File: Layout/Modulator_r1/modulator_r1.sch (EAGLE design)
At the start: 86 parts, among them Q1 FA-20H, U1 ATMEGA328P-AU, U2 TPS79933QDDCRQ1, U3 CC1125RHBT, U4 MCP1700T-3302E/TT, U5 FT232RL, U6 SIP32509DT-T1-GE3

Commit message: Add DTR coupling to reset. Closes #9.
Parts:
- added C34: 100nF, resistor:C-EUC0603
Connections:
- new net N$20: C34.2, U5.!DTR
- net AVR_NRESET: now also C34.1
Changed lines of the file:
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@@
 <grid distance="0.1" unitdist="inch" unit="inch" style="lines" multiple="1" display="no" altdistance="0.01" altunitdist="inch" altunit="inch"/>
 <layers>
-<layer number="1" name="Top" color="4" fill="1" visible="yes" active="no"/>
-<layer number="16" name="Bottom" color="1" fill="1" visible="yes" active="no"/>
-<layer number="17" name="Pads" color="2" fill="1" visible="yes" active="no"/>
-<layer number="18" name="Vias" color="2" fill="1" visible="yes" active="no"/>
-<layer number="19" name="Unrouted" color="6" fill="1" visible="yes" active="no"/>
-<layer number="20" name="Dimension" color="15" fill="1" visible="yes" active="no"/>
-<layer number="21" name="tPlace" color="7" fill="1" visible="yes" active="no"/>
-<layer number="22" name="bPlace" color="7" fill="1" visible="yes" active="no"/>
-<layer number="23" name="tOrigins" color="15" fill="1" visible="yes" active="no"/>
-<layer number="24" name="bOrigins" color="15" fill="1" visible="yes" active="no"/>
-<layer number="25" name="tNames" color="7" fill="1" visible="yes" active="no"/>
-<layer number="26" name="bNames" color="7" fill="1" visible="yes" active="no"/>
-<layer number="27" name="tValues" color="7" fill="1" visible="yes" active="no"/>
-<layer number="28" name="bValues" color="7" fill="1" visible="yes" active="no"/>
+<layer number="1" name="Top" color="4" fill="1" visible="no" active="no"/>
+<layer number="16" name="Bottom" color="1" fill="1" visible="no" active="no"/>
+<layer number="17" name="Pads" color="2" fill="1" visible="no" active="no"/>
+<layer number="18" name="Vias" color="2" fill="1" visible="no" active="no"/>
+<layer number="19" name="Unrouted" color="6" fill="1" visible="no" active="no"/>
+<layer number="20" name="Dimension" color="15" fill="1" visible="no" active="no"/>
+<layer number="21" name="tPlace" color="7" fill="1" visible="no" active="no"/>
+<layer number="22" name="bPlace" color="7" fill="1" visible="no" active="no"/>
+<layer number="23" name="tOrigins" color="15" fill="1" visible="no" active="no"/>
+<layer number="24" name="bOrigins" color="15" fill="1" visible="no" active="no"/>
+<layer number="25" name="tNames" color="7" fill="1" visible="no" active="no"/>
+<layer number="26" name="bNames" color="7" fill="1" visible="no" active="no"/>
+<layer number="27" name="tValues" color="7" fill="1" visible="no" active="no"/>
+<layer number="28" name="bValues" color="7" fill="1" visible="no" active="no"/>
 <layer number="29" name="tStop" color="7" fill="3" visible="no" active="no"/>
 <layer number="30" name="bStop" color="7" fill="6" visible="no" active="no"/>
@@
 <layer number="35" name="tGlue" color="7" fill="4" visible="no" active="no"/>
 <layer number="36" name="bGlue" color="7" fill="5" visible="no" active="no"/>
-<layer number="37" name="tTest" color="7" fill="1" visible="yes" active="no"/>
-<layer number="38" name="bTest" color="7" fill="1" visible="yes" active="no"/>
+<layer number="37" name="tTest" color="7" fill="1" visible="no" active="no"/>
+<layer number="38" name="bTest" color="7" fill="1" visible="no" active="no"/>
 <layer number="39" name="tKeepout" color="4" fill="11" visible="no" active="no"/>
 <layer number="40" name="bKeepout" color="1" fill="11" visible="no" active="no"/>
@@
 <layer number="44" name="Drills" color="7" fill="1" visible="no" active="no"/>
 <layer number="45" name="Holes" color="7" fill="1" visible="no" active="no"/>
-<layer number="46" name="Milling" color="3" fill="1" visible="yes" active="no"/>
-<layer number="47" name="Measures" color="7" fill="1" visible="yes" active="no"/>
-<layer number="48" name="Document" color="7" fill="1" visible="yes" active="no"/>
-<layer number="49" name="Reference" color="7" fill="1" visible="yes" active="no"/>
-<layer number="50" name="dxf" color="7" fill="1" visible="yes" active="no"/>
-<layer number="51" name="tDocu" color="7" fill="1" visible="yes" active="no"/>
-<layer number="52" name="bDocu" color="7" fill="1" visible="yes" active="no"/>
-<layer number="53" name="tGND_GNDA" color="7" fill="9" visible="yes" active="no"/>
-<layer number="54" name="bGND_GNDA" color="1" fill="9" visible="yes" active="no"/>
-<layer number="56" name="wert" color="7" fill="1" visible="yes" active="no"/>
-<layer number="57" name="tCAD" color="7" fill="1" visible="yes" active="no"/>
+<layer number="46" name="Milling" color="3" fill="1" visible="no" active="no"/>
+<layer number="47" name="Measures" color="7" fill="1" visible="no" active="no"/>
+<layer number="48" name="Document" color="7" fill="1" visible="no" active="no"/>
+<layer number="49" name="Reference" color="7" fill="1" visible="no" active="no"/>
+<layer number="50" name="dxf" color="7" fill="1" visible="no" active="no"/>
+<layer number="51" name="tDocu" color="7" fill="1" visible="no" active="no"/>
+<layer number="52" name="bDocu" color="7" fill="1" visible="no" active="no"/>
+<layer number="53" name="tGND_GNDA" color="7" fill="9" visible="no" active="no"/>
+<layer number="54" name="bGND_GNDA" color="1" fill="9" visible="no" active="no"/>
+<layer number="56" name="wert" color="7" fill="1" visible="no" active="no"/>
+<layer number="57" name="tCAD" color="7" fill="1" visible="no" active="no"/>
 <layer number="90" name="Modules" color="5" fill="1" visible="yes" active="yes"/>
 <layer number="91" name="Nets" color="2" fill="1" visible="yes" active="yes"/>
@@
 <part name="GPIO2" library="testpad" deviceset="PTR1" device="B1,27"/>
 <part name="GPIO3" library="testpad" deviceset="PTR1" device="B1,27"/>
+<part name="C34" library="resistor" deviceset="C-EU" device="C0603" value="100nF"/>
 </parts>
 <sheets>
@@
 <instance part="GPIO2" gate="G$1" x="-127" y="-33.02" rot="R90"/>
 <instance part="GPIO3" gate="G$1" x="-127" y="-38.1" rot="R90"/>
+<instance part="C34" gate="G$1" x="-2.54" y="48.26" rot="R270"/>
 </instances>
 <busses>
@@
 <wire x1="152.4" y1="-12.7" x2="137.16" y2="-12.7" width="0.1524" layer="91"/>
 <label x="137.16" y="-12.7" size="1.778" layer="95"/>
+</segment>
+<segment>
+<pinref part="C34" gate="G$1" pin="1"/>
+<wire x1="0" y1="48.26" x2="12.7" y2="48.26" width="0.1524" layer="91"/>
+<label x="0" y="48.26" size="1.778" layer="95"/>
 </segment>
 </net>
@@
 </segment>
 </net>
+<net name="N$20" class="0">
+<segment>
+<pinref part="C34" gate="G$1" pin="2"/>
+<pinref part="U5" gate="1" pin="!DTR"/>
+<wire x1="-7.62" y1="48.26" x2="-12.7" y2="48.26" width="0.1524" layer="91"/>
+</segment>
+</net>

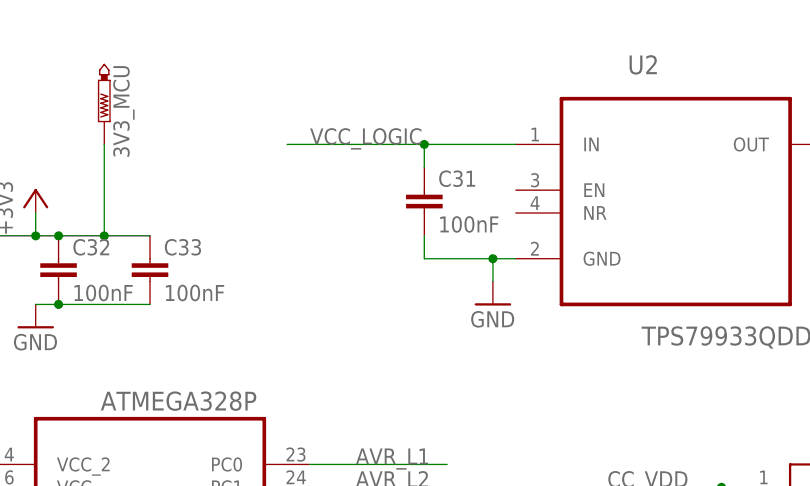
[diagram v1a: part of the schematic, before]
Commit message: Complete LDO circuit.
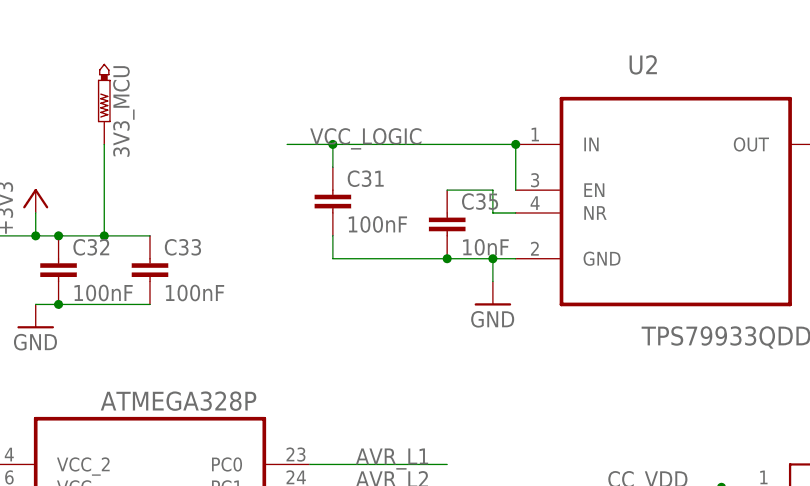
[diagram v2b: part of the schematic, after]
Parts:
- added C35: 10nF, resistor:C-EUC0603
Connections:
- new net N$30: C35.1, U2.NR
- net GND: now also C35.2
- net VCC_LOGIC: now also U2.EN
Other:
- moved on the sheet: C31
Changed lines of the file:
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@@
 <part name="GPIO3" library="testpad" deviceset="PTR1" device="B1,27"/>
 <part name="C34" library="resistor" deviceset="C-EU" device="C0603" value="100nF"/>
+<part name="C35" library="resistor" deviceset="C-EU" device="C0603" value="10nF"/>
 </parts>
 <sheets>
@@
 <instance part="R5" gate="G$1" x="53.34" y="-12.7" rot="R90"/>
 <instance part="R6" gate="G$1" x="60.96" y="-12.7" rot="R90"/>
-<instance part="C31" gate="G$1" x="73.66" y="91.44"/>
+<instance part="C31" gate="G$1" x="63.5" y="91.44"/>
 <instance part="C32" gate="G$1" x="33.02" y="83.82"/>
 <instance part="C33" gate="G$1" x="43.18" y="83.82"/>
@@
 <instance part="GPIO3" gate="G$1" x="-127" y="-38.1" rot="R90"/>
 <instance part="C34" gate="G$1" x="-2.54" y="48.26" rot="R270"/>
+<instance part="C35" gate="G$1" x="76.2" y="88.9"/>
 </instances>
 <busses>
@@
 <wire x1="81.28" y1="83.82" x2="83.82" y2="83.82" width="0.1524" layer="91"/>
 <pinref part="C31" gate="G$1" pin="2"/>
-<wire x1="81.28" y1="83.82" x2="73.66" y2="83.82" width="0.1524" layer="91"/>
-<wire x1="73.66" y1="83.82" x2="73.66" y2="86.36" width="0.1524" layer="91"/>
+<wire x1="81.28" y1="83.82" x2="76.2" y2="83.82" width="0.1524" layer="91"/>
+<wire x1="76.2" y1="83.82" x2="63.5" y2="83.82" width="0.1524" layer="91"/>
+<wire x1="63.5" y1="83.82" x2="63.5" y2="86.36" width="0.1524" layer="91"/>
 <junction x="81.28" y="83.82"/>
+<pinref part="C35" gate="G$1" pin="2"/>
+<junction x="76.2" y="83.82"/>
 </segment>
 <segment>
@@
 <segment>
 <pinref part="U2" gate="A" pin="IN"/>
-<wire x1="58.42" y1="96.52" x2="73.66" y2="96.52" width="0.1524" layer="91"/>
+<wire x1="58.42" y1="96.52" x2="63.5" y2="96.52" width="0.1524" layer="91"/>
 <label x="60.96" y="96.52" size="1.778" layer="95"/>
 <pinref part="C31" gate="G$1" pin="1"/>
-<wire x1="73.66" y1="96.52" x2="83.82" y2="96.52" width="0.1524" layer="91"/>
-<wire x1="73.66" y1="93.98" x2="73.66" y2="96.52" width="0.1524" layer="91"/>
-<junction x="73.66" y="96.52"/>
+<wire x1="63.5" y1="96.52" x2="83.82" y2="96.52" width="0.1524" layer="91"/>
+<wire x1="63.5" y1="93.98" x2="63.5" y2="96.52" width="0.1524" layer="91"/>
+<junction x="63.5" y="96.52"/>
+<pinref part="U2" gate="A" pin="EN"/>
+<wire x1="83.82" y1="91.44" x2="83.82" y2="96.52" width="0.1524" layer="91"/>
+<junction x="83.82" y="96.52"/>
 </segment>
 </net>
@@
 </segment>
 </net>
+<net name="N$30" class="0">
+<segment>
+<pinref part="C35" gate="G$1" pin="1"/>
+<wire x1="76.2" y1="91.44" x2="81.28" y2="91.44" width="0.1524" layer="91"/>
+<wire x1="81.28" y1="91.44" x2="81.28" y2="88.9" width="0.1524" layer="91"/>
+<pinref part="U2" gate="A" pin="NR"/>
+<wire x1="81.28" y1="88.9" x2="83.82" y2="88.9" width="0.1524" layer="91"/>
+</segment>
+</net>

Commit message: Add test fw.
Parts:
- R10, R7, R8, R9: value (none) -> 10K
- R3, R4, R5, R6: value (none) -> 68R
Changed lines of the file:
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@@
 <part name="VCC6" library="supply1" deviceset="VCCIO" device=""/>
 <part name="C30" library="resistor" deviceset="C-EU" device="C0603" value="100nF"/>
-<part name="R3" library="resistor" deviceset="R-EU_" device="R0603"/>
-<part name="R4" library="resistor" deviceset="R-EU_" device="R0603"/>
-<part name="R5" library="resistor" deviceset="R-EU_" device="R0603"/>
-<part name="R6" library="resistor" deviceset="R-EU_" device="R0603"/>
+<part name="R3" library="resistor" deviceset="R-EU_" device="R0603" value="68R"/>
+<part name="R4" library="resistor" deviceset="R-EU_" device="R0603" value="68R"/>
+<part name="R5" library="resistor" deviceset="R-EU_" device="R0603" value="68R"/>
+<part name="R6" library="resistor" deviceset="R-EU_" device="R0603" value="68R"/>
 <part name="C31" library="resistor" deviceset="C-EU" device="C0603" value="100nF"/>
 <part name="C32" library="resistor" deviceset="C-EU" device="C0603" value="100nF"/>
@@
 <part name="S5" library="SparkFun-Electromechanical" deviceset="SWITCH-MOMENTARY-2" device="PTH"/>
 <part name="GND18" library="supply1" deviceset="GND" device=""/>
-<part name="R7" library="resistor" deviceset="R-EU_" device="R0603"/>
-<part name="R8" library="resistor" deviceset="R-EU_" device="R0603"/>
-<part name="R9" library="resistor" deviceset="R-EU_" device="R0603"/>
-<part name="R10" library="resistor" deviceset="R-EU_" device="R0603"/>
+<part name="R7" library="resistor" deviceset="R-EU_" device="R0603" value="10K"/>
+<part name="R8" library="resistor" deviceset="R-EU_" device="R0603" value="10K"/>
+<part name="R9" library="resistor" deviceset="R-EU_" device="R0603" value="10K"/>
+<part name="R10" library="resistor" deviceset="R-EU_" device="R0603" value="10K"/>
 <part name="GND19" library="supply1" deviceset="GND" device=""/>
 <part name="+3V4" library="supply1" deviceset="+3V3" device=""/>
